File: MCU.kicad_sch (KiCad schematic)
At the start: 29 parts, among them U25 STM32H743VITx, Y1 8MHz

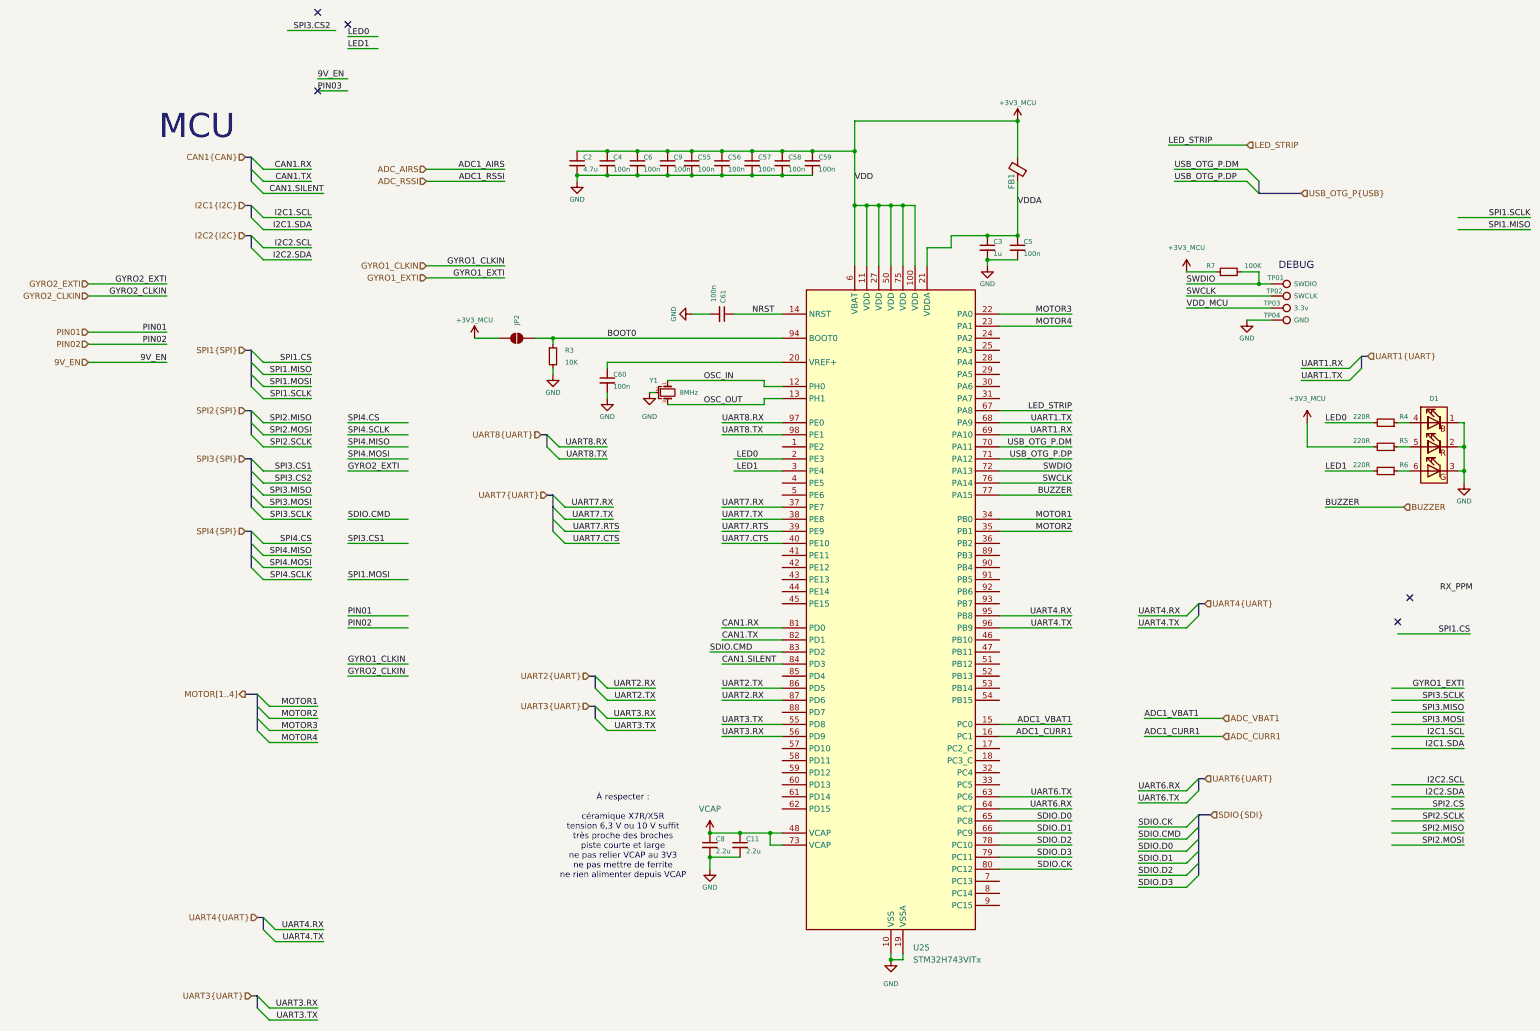
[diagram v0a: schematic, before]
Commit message: rework and work on IMUs
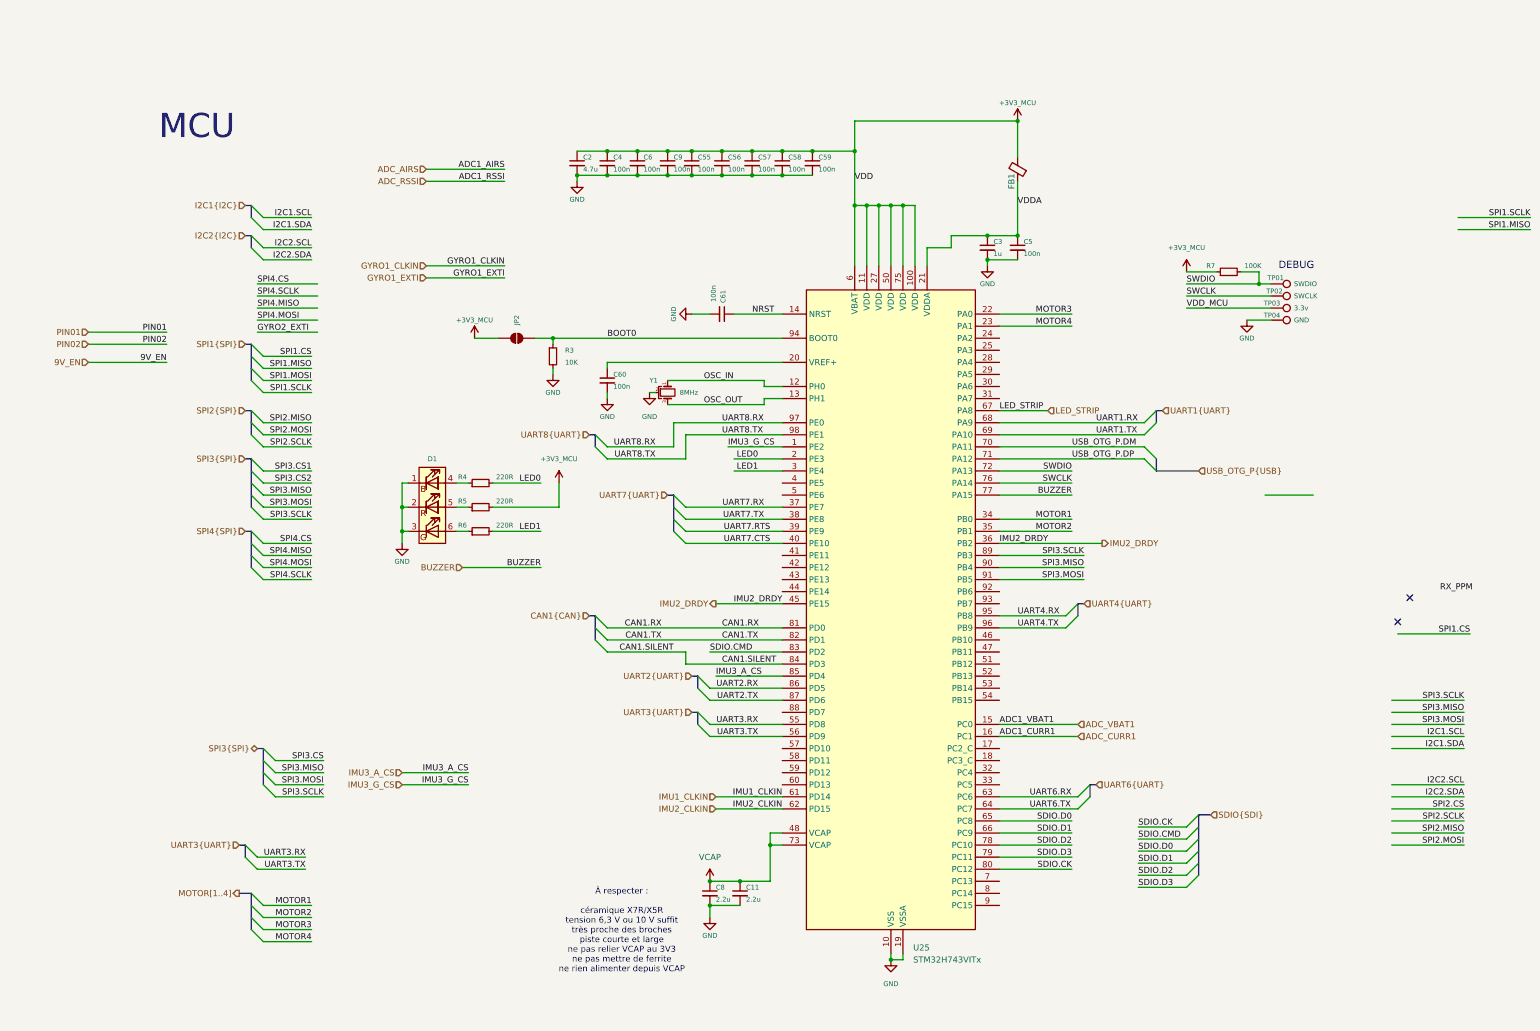
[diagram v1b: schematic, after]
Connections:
- net SPI3.MISO: now also U25.90 (PB4)
- net SPI3.MOSI: now also U25.91 (PB5)
- net SPI3.SCLK: now also U25.89 (PB3)
- net UART1.RX: now also U25.68 (PA9); no longer U25.69 (PA10)
- net UART1.TX: now also U25.69 (PA10); no longer U25.68 (PA9)
- net UART2.RX: now also U25.86 (PD5); no longer U25.87 (PD6)
- net UART2.TX: now also U25.87 (PD6); no longer U25.86 (PD5)
- net UART3.RX: now also U25.55 (PD8); no longer U25.56 (PD9)
- net UART3.TX: now also U25.56 (PD9); no longer U25.55 (PD8)
- net UART6.RX: now also U25.63 (PC6); no longer U25.64 (PC7)
- net UART6.TX: now also U25.64 (PC7); no longer U25.63 (PC6)
- net IMU3_G_CS: now reaches U25.1 (PE2)
- net IMU2_DRDY: now reaches U25.36 (PB2)
- net IMU2_DRDY: now also U25.45 (PE15)
- net IMU1_CLKIN: now reaches U25.61 (PD14)
- net IMU2_CLKIN: now reaches U25.62 (PD15)
- net IMU3_A_CS: now reaches U25.85 (PD4)
- no-connect marks 5 -> 2
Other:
- moved on the sheet: C11, C8

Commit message: update name
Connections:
- net ADC_VBAT2: now reaches U25.28 (PA4)
- net ADC_AIRSPEED: now reaches U25.32 (PC4)
- no-connect marks 2 -> 0
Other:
- note removed: "MCU"
- company: Pierluigi Colangeli, PhD -> (none)
- title: LEVIA H7 -> (none)

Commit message: upsadte SPI4 set to Baro
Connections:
- net SPI2.MISO: now also U25.53 (PB14)
- net SPI2.MOSI: now also U25.54 (PB15)
- net SPI2.SCLK: now also U25.52 (PB13)
- net 9V_EN: now reaches U25.4 (PE5)
- net SPI2.CS: now reaches U25.51 (PB12)
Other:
- note added: "PB12 = BMP581_CS PB13 = SPI2_SCK PB14 = SPI2_MISO PB15 = SPI2_MOSI"
- title: (none) -> H743_ARDUPILOT
- moved on the sheet: D1, R4, R5, R6

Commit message: remove 9v_EN 9v power supply alwaye activated
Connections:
- net 9V_EN: no longer names the net of U25.4 (PE5)
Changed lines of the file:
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@@
 	(wire
 		(pts
-			(xy 135.89 93.98) (xy 146.05 93.98)
-		)
-		(stroke
-			(width 0)
-			(type default)
-		)
-	)
-	(wire
-		(pts
 			(xy 231.14 176.53) (xy 220.98 176.53)
 		)
@@
 		(effects
 			(font
-				(size 1.27 1.27)
-			)
-			(justify left bottom)
-		)
-	)
-	(label "9V_EN"
-		(at 135.89 93.98 0)
-		(effects
-			(font

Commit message: re annotate componant globaly
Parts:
- renumbered C2 to C1, C11 to C10, C57 to C11, C58 to C12, C59 to C13, C3 to C14, C5 to C15, C4 to C2, C60 to C3, C6 to C4, C9 to C5, C55 to C6, C8 to C7, C56 to C8, C61 to C9, JP2 to JP1, R4 to R3, R5 to R4, R6 to R5, R3 to R6, TP01 to TP1, TP02 to TP2, TP03 to TP3, TP04 to TP4, U25 to U2

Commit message: solved issue on SPI1
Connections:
- net IMU2_DRDY: no longer U2.45 (PE15)
- net SPI1.MISO: now also U2.30 (PA6)
- net SPI1.MOSI: now also U2.31 (PA7)
- net SPI1.SCLK: now also U2.29 (PA5)
- new net IMU1_DRDY: U2.45 (PE15)
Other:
- note removed: "PB12 = BMP581_CS PB13 = SPI2_SCK PB14 = SPI2_MISO PB15 = SPI2_MOSI"

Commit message: fix VREF+ supply and complete SPI1 wiring
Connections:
- net SPI1.CS: now also U2.9 (PC15)
- net SPI1.MOSI: now also U2.88 (PD7)
- net VDDA: now also C3.1, U2.20 (VREF+)
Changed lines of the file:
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@@
 	(wire
 		(pts
+			(xy 135.89 142.24) (xy 146.05 142.24)
+		)
+		(stroke
+			(width 0)
+			(type default)
+		)
+	)
+	(wire
+		(pts
+			(xy 191.77 182.88) (xy 207.01 182.88)
+		)
+		(stroke
+			(width 0)
+			(type default)
+		)
+	)
+	(wire
+		(pts
 			(xy 109.22 29.21) (xy 115.57 29.21)
 		)
@@
 		)
 	)
+	(label "SPI1.MOSI"
+		(at 135.89 142.24 180)
+		(effects
+			(font
+				(size 1.27 1.27)
+			)
+			(justify right bottom)
+		)
+	)
+	(label "SPI1.CS"
+		(at 207.01 182.88 0)
+		(effects
+			(font
+				(size 1.27 1.27)
+			)
+			(justify left bottom)
+		)
+	)
+	(label "VDDA"
+		(at 109.22 68.58 180)
+		(effects
+			(font
+				(size 1.27 1.27)
+			)
+			(justify right bottom)
+		)
+	)

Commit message: audit DigiKey metadata: MCU.kicad_sch
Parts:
- C1: DigiKey Part Number (none) -> 1276-1482-1-ND; DigiKey Price Qty (none) -> 1 CT; DigiKey Specs (none) -> 4.7 µF ±20%, 10 V, X5R, 0402; DigiKey Status (none) -> Active; no stock at audit; DigiKey URL (none) -> https://www.digikey.fr/en/products/detail/samsung-electro-m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; DigiKey Unit Price EUR (none) -> 0.09; Footprint Audit (none) -> OK; LCSC C23733 -> (none); LCSC Part C23733 -> (none); Library Audit (none) -> KiCad standard; Package (none) -> 0402 (1005); Price Checked (none) -> 2026-09-25
- C10, C7: DigiKey Part Number (none) -> 445-9076-1-ND; DigiKey Price Qty (none) -> 1 CT; DigiKey Specs (none) -> 2.2 µF ±20%, 16 V, X5R, 0402; DigiKey Status (none) -> Active upgrade; DigiKey URL (none) -> https://www.digikey.fr/en/products/result?keywords=C1005X5R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; DigiKey Unit Price EUR (none) -> 0.27; Footprint Audit (none) -> OK; LCSC C12530 -> (none); LCSC Part C12530 -> (none); Library Audit (none) -> KiCad standard; MPN CL05A225MQ5NSNC -> C1005X5R1C225M050BC; Manufacturer Samsung Electro-Mechanics -> TDK; Package (none) -> 0402 (1005); Price Checked (none) -> 2026-09-25
- C11, C12, C13, C15, C2, C3, C4, C5, C6, C8, C9: DigiKey Part Number (none) -> 1276-1001-1-ND; DigiKey Price Qty (none) -> 1 CT; DigiKey Specs (none) -> 100 nF ±10%, 16 V, X7R, 0402; DigiKey Status (none) -> Active; DigiKey URL (none) -> https://www.digikey.fr/fr/products/detail/samsung-electro-m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; DigiKey Unit Price EUR (none) -> 0.09; Footprint Audit (none) -> OK; LCSC C1525 -> (none); LCSC Part C1525 -> (none); Library Audit (none) -> KiCad standard; MPN GRM022R60J104KE15D -> CL05B104KO5NNNC; Manufacturer Murata Electronics -> Samsung Electro-Mechanics; Package (none) -> 0402 (1005); Price Checked (none) -> 2026-09-25
- C14: DigiKey Part Number (none) -> 1276-1445-1-ND; DigiKey Price Qty (none) -> 1 CT; DigiKey Specs (none) -> 1 µF ±10%, 25 V, X5R, 0402; DigiKey Status (none) -> Active; DigiKey URL (none) -> https://www.digikey.fr/en/products/result?keywords=CL05A105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; DigiKey Unit Price EUR (none) -> 0.16; Footprint Audit (none) -> OK; LCSC C52923 -> (none); LCSC Part C52923 -> (none); Library Audit (none) -> KiCad standard; Package (none) -> 0402 (1005); Price Checked (none) -> 2026-09-25
- D1: DigiKey Specs (none) -> RGB LED, 6-pin SMD 1.6x1.6 mm class; DigiKey Status (none) -> No exact DigiKey listing confirmed; LCSC source retained; DigiKey URL (none) -> https://www.digikey.fr/en/products/result?keywords=19-337%2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; Footprint Audit (none) -> CHECK supplier drawing before release; Library Audit (none) -> Embedded symbol + EasyEDA footprint; Manufacturer EVERLIGHT(亿光) -> Everlight Electronics; Package (none) -> 6-SMD RGB LED 1.6x1.6 mm; Price Checked (none) -> 2026-09-25
- FB1: DigiKey Part Number (none) -> 490-1006-1-ND; DigiKey Price Qty (none) -> 1 CT; DigiKey Specs (none) -> 600 Ω @100 MHz, 300 mA, 0402; DigiKey Status (none) -> Active; DigiKey URL (none) -> https://www.digikey.fr/fr/products/detail/murata-electronic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; DigiKey Unit Price EUR (none) -> 0.09; Footprint Audit (none) -> OK; LCSC C127281 -> (none); LCSC Part C127281 -> (none); Library Audit (none) -> KiCad standard; MPN FCM1608KF-601T02 -> BLM15AG601SN1D; Manufacturer TAI-TECH -> Murata Electronics; Package (none) -> 0402 (1005); Price Checked (none) -> 2026-09-25
- JP1: DigiKey Price Qty (none) -> N/A; DigiKey Status (none) -> PCB feature / no purchased component; DigiKey Unit Price EUR (none) -> 0; Footprint Audit (none) -> CHECK: _pico footprint library not present in repository; Library Audit (none) -> External unresolved footprint library; Package (none) -> PCB solder jumper; Price Checked (none) -> 2026-09-25
- R3, R4, R5: DigiKey Specs (none) -> 220 Ω ±1%, 0402; DigiKey Status (none) -> Active / family verified; DigiKey URL (none) -> https://www.digikey.fr/en/products/result?keywords=RC0402FR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; Footprint Audit (none) -> OK; LCSC C25091 -> (none); LCSC Part C25091 -> (none); Library Audit (none) -> KiCad standard; MPN 0402WGF2200TCE -> RC0402FR-07220RL; Manufacturer UNI-ROYAL(Uniroyal Elec) -> YAGEO; Package (none) -> 0402 (1005); Price Checked (none) -> 2026-09-25
- R6: DigiKey Price Qty (none) -> 1 CT; DigiKey Specs (none) -> 10 kΩ ±1%, 0402; DigiKey Status (none) -> Active / family verified; DigiKey URL (none) -> https://www.digikey.fr/en/products/result?keywords=RC0402FR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; DigiKey Unit Price EUR (none) -> 0.09; Footprint Audit (none) -> OK; LCSC C25744 -> (none); LCSC Part C25744 -> (none); Library Audit (none) -> KiCad standard; MPN 0402WGF1002TCE -> RC0402FR-0710KL; Manufacturer UNI-ROYAL(Uniroyal Elec) -> YAGEO; Package (none) -> 0402 (1005); Price Checked (none) -> 2026-09-25
- R7: DigiKey Price Qty (none) -> 1 CT; DigiKey Specs (none) -> 100 kΩ ±1%, 0402; DigiKey Status (none) -> Active / family verified; DigiKey URL (none) -> https://www.digikey.fr/en/products/result?keywords=RC0402FR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; DigiKey Unit Price EUR (none) -> 0.09; Footprint Audit (none) -> OK; LCSC C25741 -> (none); LCSC Part C25741 -> (none); Library Audit (none) -> KiCad standard; MPN 0402WGF1003TCE -> RC0402FR-07100KL; Manufacturer UNI-ROYAL(Uniroyal Elec) -> YAGEO; Package (none) -> 0402 (1005); Price Checked (none) -> 2026-09-25
- TP1, TP2, TP3, TP4: DigiKey Price Qty (none) -> N/A; DigiKey Status (none) -> PCB feature / no purchased component; DigiKey Unit Price EUR (none) -> 0; Footprint Audit (none) -> TBD: no footprint assigned; Library Audit (none) -> KiCad TestPoint symbol; Package (none) -> PCB test pad; Price Checked (none) -> 2026-09-25
- U2: value STM32H743VITx -> STM32H743VIT6; DigiKey Part Number (none) -> 497-17720-ND; DigiKey Price Qty (none) -> 1 CT; DigiKey Specs (none) -> Cortex-M7 480 MHz, 2 MB Flash, 1 MB RAM, LQFP-100 14x14 P0.5; DigiKey Status (none) -> Active; DigiKey URL (none) -> https://www.digikey.fr/en/products/detail/stmicroelectronic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; DigiKey Unit Price EUR (none) -> 14.27; Footprint Audit (none) -> OK; Library Audit (none) -> KiCad standard; MPN (none) -> STM32H743VIT6; Manufacturer (none) -> STMicroelectronics; Package (none) -> LQFP-100 14x14 mm P0.5; Price Checked (none) -> 2026-09-25
- Y1: DigiKey Price Qty (none) -> 1 CT; DigiKey Specs (none) -> 8 MHz CERALOCK, built-in 33 pF, 3-SMD 3.2x1.3 mm; DigiKey Status (none) -> Active; DigiKey URL (none) -> https://www.digikey.fr/en/products/result?keywords=CSTNE8M0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; DigiKey Unit Price EUR (none) -> 0.26; Footprint Audit (none) -> OK by package geometry; Library Audit (none) -> External EasyEDA footprint; Manufacturer muRata(村田) -> Murata Electronics; Package (none) -> 3-SMD 3.2x1.3 mm; Price Checked (none) -> 2026-09-25
